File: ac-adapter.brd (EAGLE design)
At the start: 98.4 x 47 mm, 67 parts, among them IC1 BM1Q011, IC2 TL431, Q1 TLP621-1, Q2 600V5A, T1 COMMON_FILTER-SU10VFC, T2 TRANSFORMAER_FLYBACK-PQ2620-2

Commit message: 発注
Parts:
- moved DR1 0.32 mm to (3.81, 2.86)
- moved DR3 0.32 mm to (95.2, 2.86)
- moved DR2 0.32 mm to (3.81, 44.8)
- moved DR4 0.32 mm to (95.2, 44.8)
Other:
- board size 98.4 x 47 mm -> 98.4 x 47.6 mm
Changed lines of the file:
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@@
 <board>
 <plain>
-<wire x1="0" y1="0" x2="0" y2="46.99" width="0.3048" layer="20"/>
-<wire x1="0" y1="46.99" x2="98.365" y2="46.99" width="0.3048" layer="20"/>
-<wire x1="98.365" y1="46.99" x2="98.365" y2="0" width="0.3048" layer="20"/>
+<wire x1="0" y1="0" x2="0" y2="47.625" width="0.3048" layer="20"/>
+<wire x1="0" y1="47.625" x2="98.365" y2="47.625" width="0.3048" layer="20"/>
+<wire x1="98.365" y1="47.625" x2="98.365" y2="0" width="0.3048" layer="20"/>
 <wire x1="98.365" y1="0" x2="0" y2="0" width="0.3048" layer="20"/>
 <text x="61.595" y="44.1325" size="1.8288" layer="21">QR AC adapter Ver 2</text>
-<dimension x1="0" y1="0" x2="0" y2="46.99" x3="-2.540003125" y3="23.495" textsize="1.778" layer="47"/>
+<dimension x1="0" y1="0" x2="0" y2="47.625" x3="-2.540003125" y3="23.8125" textsize="1.778" layer="47"/>
 <wire x1="52.07" y1="0" x2="52.07" y2="13.97" width="0.8128" layer="21"/>
 <wire x1="52.07" y1="13.97" x2="54.61" y2="16.51" width="0.8128" layer="21"/>
@@
 <attribute name="VALUE" x="20.47875" y="29.62275" size="1.016" layer="27" ratio="10" rot="R90"/>
 </element>
-<element name="DR1" library="my_connector" package="HOLE_3.2" value="HOLE-3.2" x="3.81" y="2.54" smashed="yes"/>
-<element name="DR2" library="my_connector" package="HOLE_3.2" value="HOLE-3.2" x="3.81" y="44.45" smashed="yes"/>
-<element name="DR3" library="my_connector" package="HOLE_3.2" value="HOLE-3.2" x="95.25" y="2.54" smashed="yes"/>
-<element name="DR4" library="my_connector" package="HOLE_3.2" value="HOLE-3.2" x="95.25" y="44.45" smashed="yes"/>
+<element name="DR1" library="my_connector" package="HOLE_3.2" value="HOLE-3.2" x="3.81" y="2.8575" smashed="yes"/>
+<element name="DR2" library="my_connector" package="HOLE_3.2" value="HOLE-3.2" x="3.81" y="44.7675" smashed="yes"/>
+<element name="DR3" library="my_connector" package="HOLE_3.2" value="HOLE-3.2" x="95.25" y="2.8575" smashed="yes"/>
+<element name="DR4" library="my_connector" package="HOLE_3.2" value="HOLE-3.2" x="95.25" y="44.7675" smashed="yes"/>
 <element name="C17" library="my_rcl" package="1608" value="1000p" x="38.89375" y="12.065" smashed="yes" rot="MR90">
 <attribute name="NAME" x="39.89375" y="10.465" size="0.8128" layer="26" rot="MR90"/>

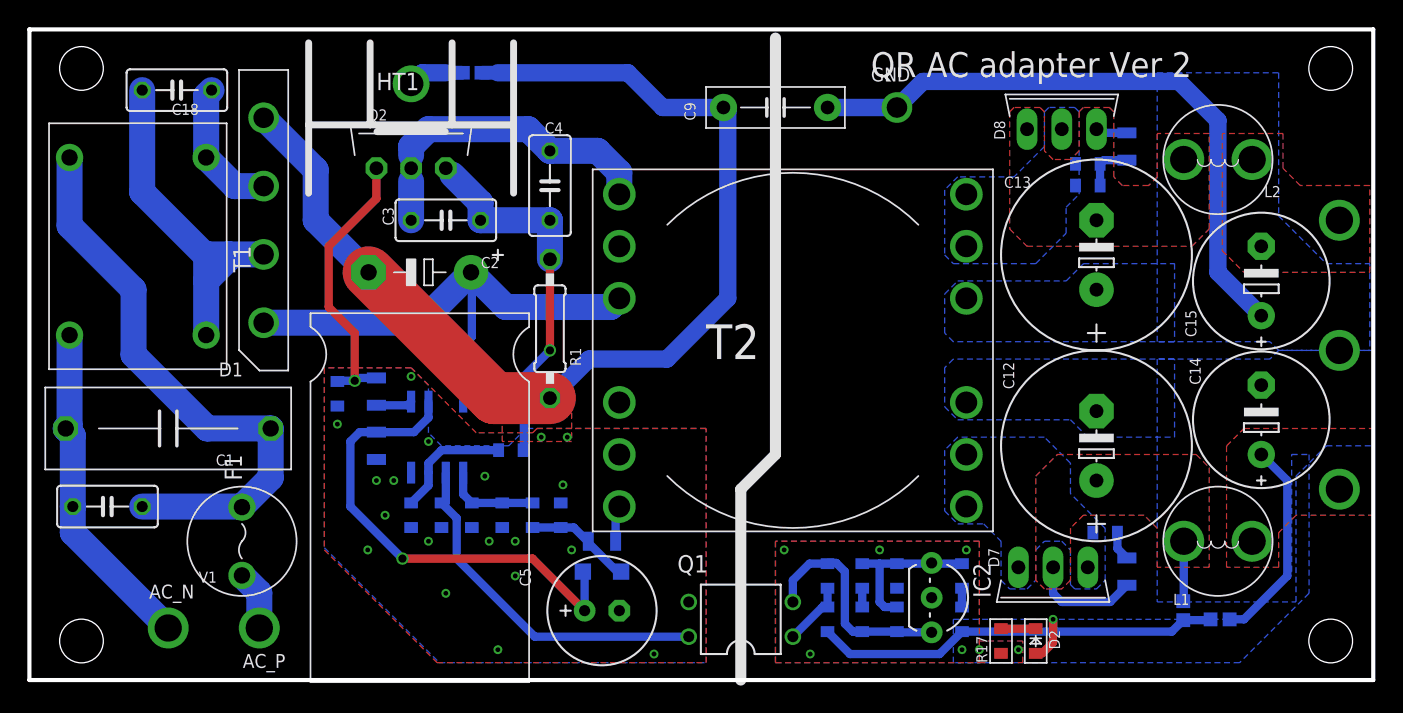
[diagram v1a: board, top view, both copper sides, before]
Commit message: PFCコントローラーを使う
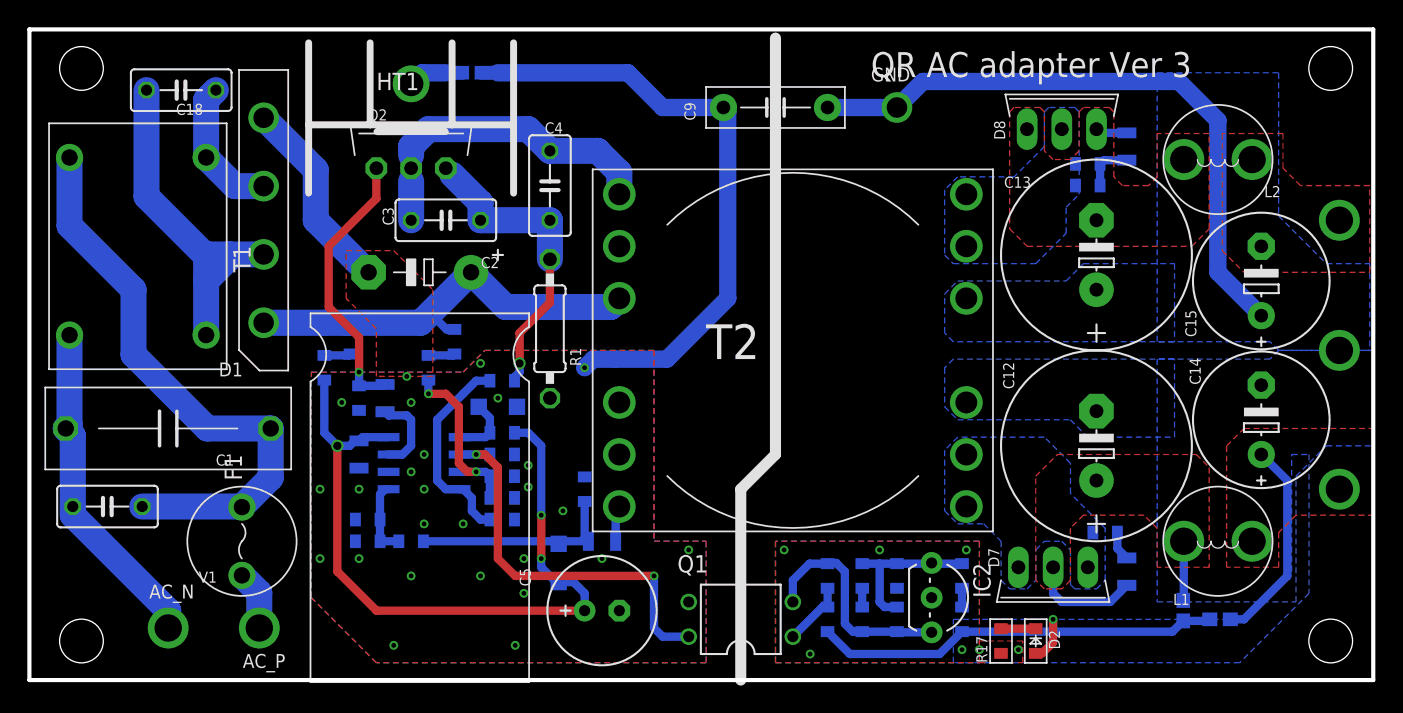
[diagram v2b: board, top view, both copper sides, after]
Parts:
- added C21: 1000p, my_rcl:1608
- added D3: 1N4148, my_rcl:SOD123
- added R19, R22: DNP, my_rcl:1608
- added R20: 100k, my_rcl:1608
- added R21, R23: 240k, my_rcl:1608
- IC1: value BM1Q011 -> NCP1608; device my_ic:SOP8-J7S -> my_ic:SOP8
- R15: value 10k -> DNP; device my_rcl:2012 -> my_rcl:1608
- R4: value 10k -> 47k
- R5: value 1.5k -> DNP
- SJ1, SJ2: device Connector_Robotech:SJ1608 -> my_rcl:1608-J
- moved R5 10.0 mm to (24.8, 10.2), turned to 180 degrees
- moved R4 9.09 mm to (27.9, 10.2), turned to 180 degrees
- moved C6 7.63 mm to (24.8, 11.7), turned to 0 degrees
- moved C19 6.68 mm to (34.6, 11.7), turned to 180 degrees
- moved C7 6.29 mm to (34.6, 16.5), turned to 180 degrees
- moved R16 5.12 mm to (34.6, 21.9)
- moved D5 3.24 mm to (38.7, 8.57), turned to 270 degrees
- moved R15 2.71 mm to (29.2, 22.9)
- moved C17 2.58 mm to (40.6, 14.0)
- moved IC1 2.13 mm to (28.9, 15.9), turned to 270 degrees
- moved R18 1.62 mm to (24.1, 20.6)
- moved C8 1.42 mm to (24.1, 16.5)
- moved R3 0.79 mm to (26.0, 20.6)
- moved C18 0.32 mm to (11.1, 43.2)
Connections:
- new net N$24: D3.1, IC1.1, R20.1
- new net N$30: R15.2, R22.1
- new net N$31: R21.2, R23.1
- net N$13: now also IC1.7; no longer IC1.5
- net N$15: now also IC1.4; no longer IC1.3
- net N$5: now also C21.1, IC1.3, R19.2; no longer IC1.8
- net N$7: now also IC1.5; no longer IC1.1
- net PGND: now also C21.2, D3.2, IC1.6, R19.1; no longer IC1.4
- net VCC: now also IC1.8, R20.2, R21.1; no longer IC1.6
- net VP: now also R22.2, R23.2; no longer R15.2
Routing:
- net PGND: track 80.5 -> 59.9 mm, vias 19 -> 26
- net VCC: track 35.6 -> 54.2 mm, vias 1 -> 3
- net N$5: track 2.43 -> 13.2 mm, vias 0 -> 2
- net N$11: track 7.88 -> 15.2 mm
- net N$15: track 8.96 -> 15.1 mm
- net N$12: track 27.6 -> 22.8 mm
- net N$24: track 0.00 -> 4.59 mm
- net N$13: track 2.65 -> 5.96 mm
- net N$19: track 26.4 -> 29.4 mm, vias 0 -> 2
- net VP: track 34.4 -> 32.2 mm
- net N$31: track 0.00 -> 1.95 mm
- net N$30: track 0.00 -> 1.95 mm
- net N$7: track 6.92 -> 5.60 mm
- net N$14: track 20.8 -> 20.2 mm
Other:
- board text added: "QR AC adapter Ver 3"
- board text removed: "QR AC adapter Ver 2"

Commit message: パターン修正
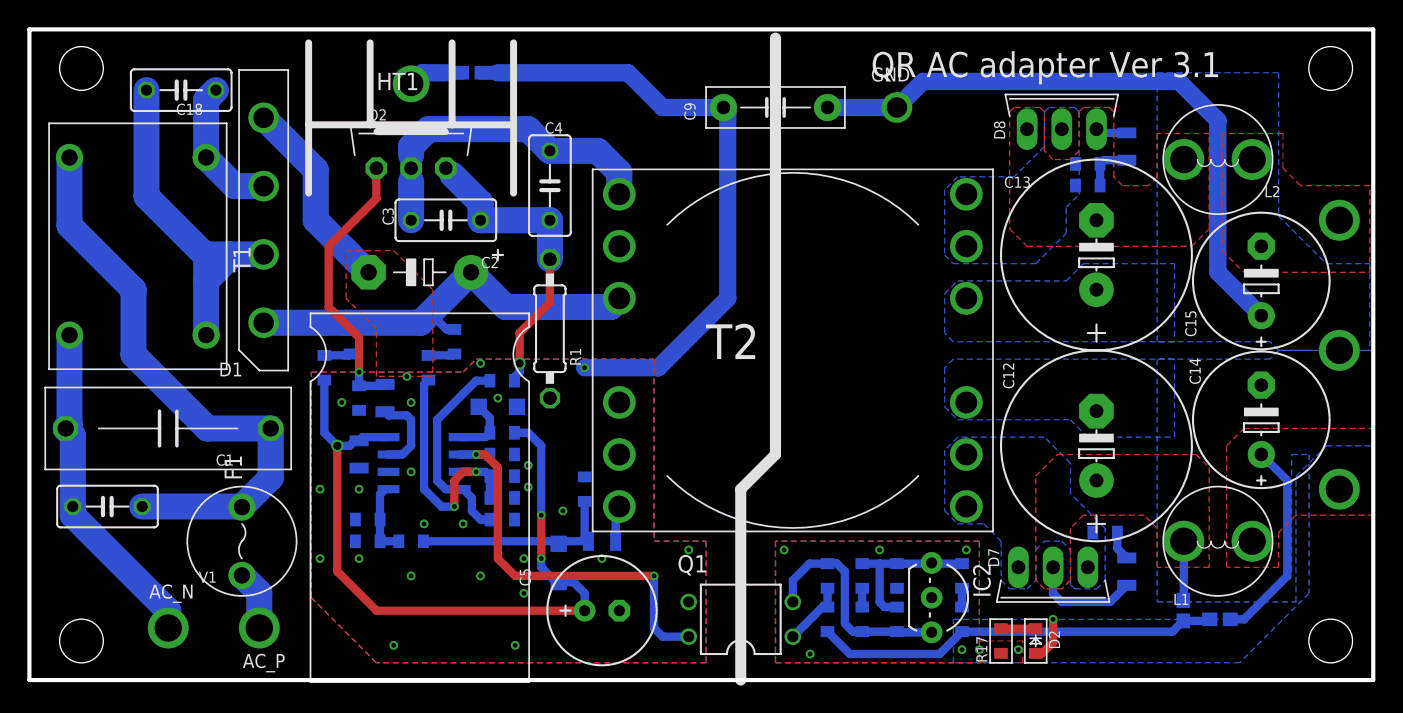
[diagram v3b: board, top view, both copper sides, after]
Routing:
- net N$5: track 13.2 -> 18.6 mm
- net PGND: vias 26 -> 24
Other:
- board text added: "QR AC adapter Ver 3.1"
- board text removed: "QR AC adapter Ver 3"

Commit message: GaNに対応
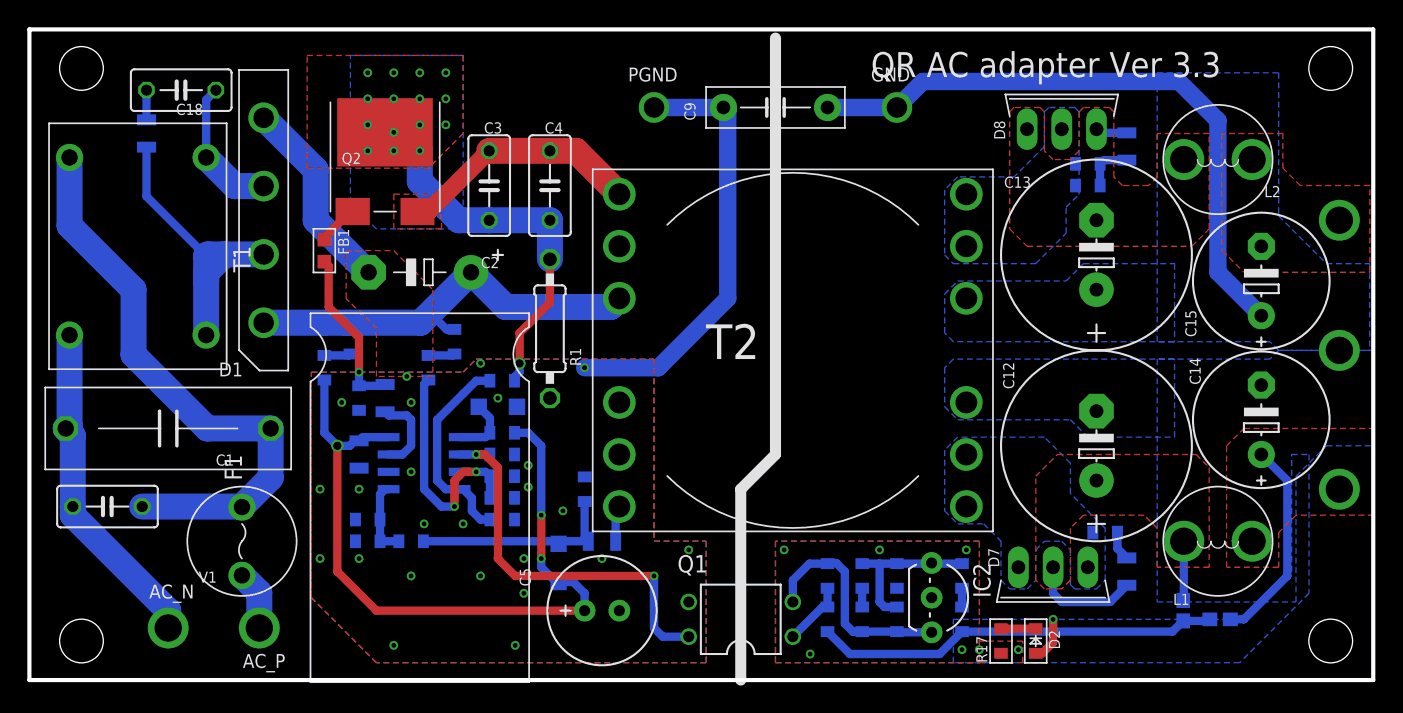
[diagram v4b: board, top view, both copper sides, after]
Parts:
- removed HT1: HEATSINK-2, my_connector:HEATSINK2
- added R24: 10, my_rcl:2012
- added TP7: PGND, my_connector:TESTPIN-BIG
- FB1: device my_rcl:1608-J -> my_rcl:1608-FB
- Q2: device my_ic:TO-220 -> my_ic:PQFN8X8
- moved FB1 16.9 mm to (21.6, 31.4), flipped to the top, turned to 270 degrees
- moved C3 4.07 mm to (33.7, 36.2), turned to 270 degrees
- moved Q2 3.70 mm to (26.0, 34.3)
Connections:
- new net N$32: C18.2, R24.2
- net N$12: now also Q2.S; no longer Q2.3
- net N$14: now also FB1.2; no longer Q2.1
- net N$20: now also Q2.G; no longer HT1.HT1
- net N$4: now also R24.1; no longer C18.2
- net PGND: now also TP7.1; no longer FB1.2
- net SW: now also Q2.D; no longer Q2.2
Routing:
- net PGND: track 59.9 -> 46.3 mm
- net N$14: track 20.2 -> 12.1 mm
- net SW: track 24.1 -> 17.9 mm
- net N$4: track 26.6 -> 22.3 mm
- net N$12: track 22.8 -> 25.8 mm, vias 1 -> 16
- net N$32: track 0.00 -> 2.17 mm
- net N$20: track 4.03 -> 3.01 mm
- added copper zone on layer 1, net N$12
- added copper zone on layer 16, net N$12
- added copper zone on layer 1, net SW
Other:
- board text added: "QR AC adapter Ver 3.3"
- board text removed: "QR AC adapter Ver 3.1"
